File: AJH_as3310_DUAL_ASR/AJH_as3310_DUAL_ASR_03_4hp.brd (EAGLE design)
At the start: 19 x 106.8 mm, 56 parts, among them IC1 LM4040 5.0V, IC2 TL072D, IC3 CEM3310SOIC16, IC4 CEM3310SOIC16, IC5 TL072D, J100 PJ301_THONKICONN6, J101 PJ301_THONKICONN6, J102 PJ301_THONKICONN6, J103 PJ301_THONKICONN6

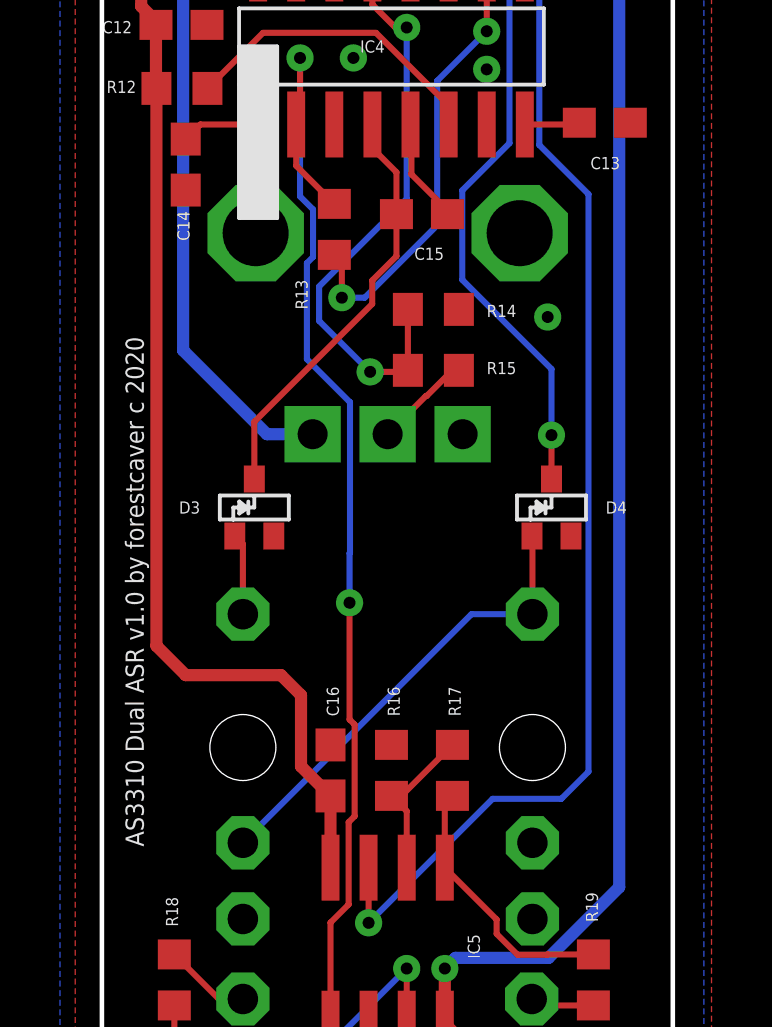
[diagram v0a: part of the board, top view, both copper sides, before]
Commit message: Fix gate input (pulldown)
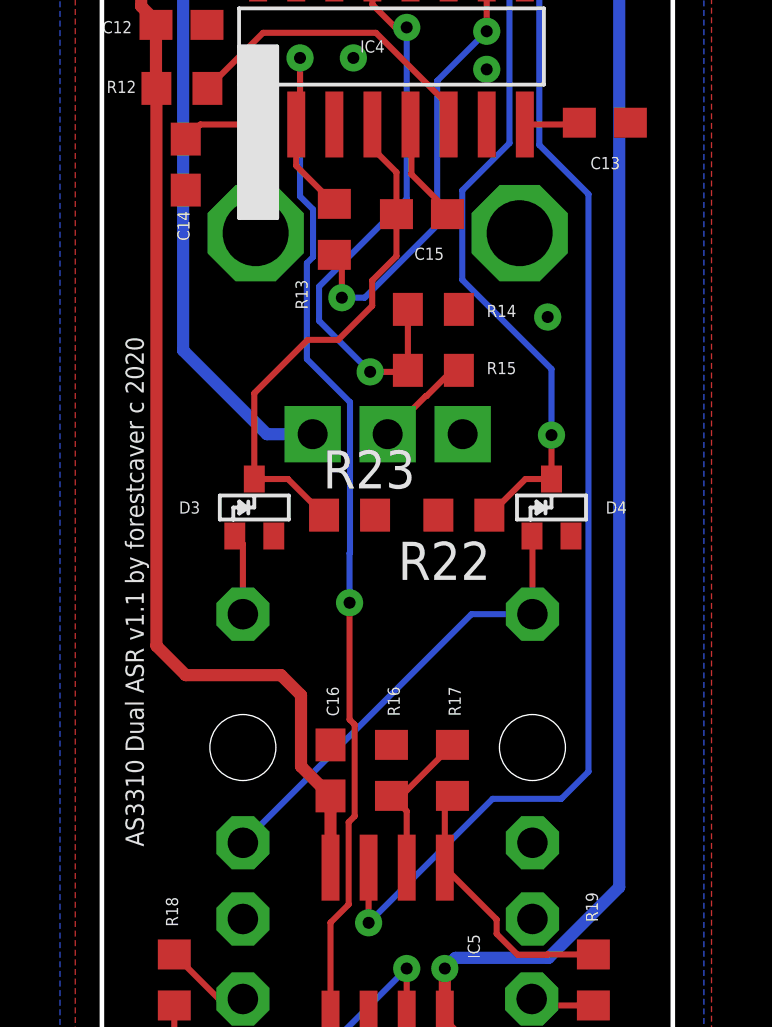
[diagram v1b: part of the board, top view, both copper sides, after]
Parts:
- added R22, R23: 100k, resistor:R0603
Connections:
- net GATE1_IN: now also R22.1
- net GATE2_IN: now also R23.1
- net GND: now also R22.2, R23.2
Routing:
- net GATE2_IN: track 14.1 -> 17.5 mm
- net GATE1_IN: track 39.9 -> 42.4 mm
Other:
- board text added: "AS3310 Dual ASR v1.1 by forestcaver c 2020"
- board text removed: "AS3310 Dual ASR v1.0 by forestcaver c 2020"
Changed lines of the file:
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@@
 <?xml version="1.0" encoding="utf-8"?>
 <!DOCTYPE eagle SYSTEM "eagle.dtd">
-<eagle version="9.5.2">
+<eagle version="9.6.2">
 <drawing>
 <settings>
@@
 <wire x1="19.03" y1="106.76" x2="0" y2="106.76" width="0.1524" layer="20"/>
 <wire x1="0" y1="106.76" x2="0" y2="0" width="0.1524" layer="20"/>
-<text x="1.397" y="16.764" size="0.6096" layer="21" rot="R90">AS3310 Dual ASR v1.0 by forestcaver c 2020</text>
+<text x="1.397" y="16.764" size="0.6096" layer="21" rot="R90">AS3310 Dual ASR v1.1 by forestcaver c 2020</text>
 </plain>
 <attributes>
@@
 <attribute name="VALUE" x="4.445" y="11.43" size="1.27" layer="27" rot="R90"/>
 </element>
+<element name="R22" library="resistor" package="R0603" value="100k" x="12.065" y="27.813" smashed="yes" rot="R180">
+<attribute name="NAME" x="12.954" y="26.924" size="1.27" layer="25" rot="R180"/>
+<attribute name="VALUE" x="12.954" y="29.845" size="1.27" layer="27" rot="R180"/>
+</element>
+<element name="R23" library="resistor" package="R0603" value="100k" x="8.255" y="27.813" smashed="yes">
+<attribute name="NAME" x="7.366" y="28.702" size="1.27" layer="25"/>
+<attribute name="VALUE" x="7.366" y="25.781" size="1.27" layer="27"/>
+</element>
 </elements>
 <signals>
@@
 <contactref element="R16" pad="1"/>
 <contactref element="R20" pad="1"/>
+<contactref element="R22" pad="2"/>
+<contactref element="R23" pad="2"/>
 </signal>
 <signal name="12V" class="1">
@@
 <contactref element="D4" pad="CATHODE"/>
 <wire x1="14.986" y1="29.017" x2="14.986" y2="30.48" width="0.2032" layer="1"/>
+<contactref element="R22" pad="1"/>
+<wire x1="12.915" y1="27.813" x2="14.119" y2="29.017" width="0.2032" layer="1"/>
+<wire x1="14.119" y1="29.017" x2="14.986" y2="29.017" width="0.2032" layer="1"/>
 </signal>
 <signal name="N$5">
@@
 <wire x1="9.0472" y1="40.8038" x2="9.017" y2="40.834" width="0.2032" layer="1"/>
 <wire x1="9.818" y1="37.846" x2="9.818" y2="36.44295" width="0.2032" layer="1"/>
-<wire x1="9.818" y1="36.44295" x2="9.0106" y2="35.63555" width="0.2032" layer="1"/>
-<wire x1="9.0106" y1="34.8526" x2="9.0106" y2="35.63555" width="0.2032" layer="1"/>
-<wire x1="5.08" y1="30.922" x2="9.0106" y2="34.8526" width="0.2032" layer="1"/>
-<wire x1="5.08" y1="29.017" x2="5.08" y2="30.922" width="0.2032" layer="1"/>
+<wire x1="9.0106" y1="35.63555" x2="9.818" y2="36.44295" width="0.2032" layer="1"/>
+<contactref element="R23" pad="1"/>
+<wire x1="5.08" y1="29.017" x2="6.201" y2="29.017" width="0.2032" layer="1"/>
+<wire x1="6.201" y1="29.017" x2="7.405" y2="27.813" width="0.2032" layer="1"/>
+<wire x1="5.08" y1="31.877" x2="6.858" y2="33.655" width="0.2032" layer="1"/>
+<wire x1="6.858" y1="33.655" x2="7.874" y2="33.655" width="0.2032" layer="1"/>
+<wire x1="7.874" y1="33.655" x2="9.0106" y2="34.7916" width="0.2032" layer="1"/>
+<wire x1="5.08" y1="29.017" x2="5.08" y2="31.877" width="0.2032" layer="1"/>
+<wire x1="9.0106" y1="34.7916" x2="9.0106" y2="35.63555" width="0.2032" layer="1"/>
 </signal>
 <signal name="A2_IN">
